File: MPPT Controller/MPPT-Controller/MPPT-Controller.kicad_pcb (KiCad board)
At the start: 4 copper layers, 89 parts, among them J1 Conn_01x02_Pin, J2 Conn_01x02_Pin, J3 Conn_01x02_Pin, J4 Conn_01x02_Pin, J5 USB_C_Receptacle_USB2.0_16P, J6 Conn_01x02_Pin, J7 Conn_01x02_Pin, J8 Conn_01x02_Pin, M1 Fan_4pin, Q1 IRL540N, SW1 SW_SPDT, U1 ADS1115IDGS, U2 ESP32-WROOM-32D, U3 CH340C, U4 LM1117DT-3.3, U5 LM2596S-ADJ, U6 TC4422, U7 ADS1115IDGS

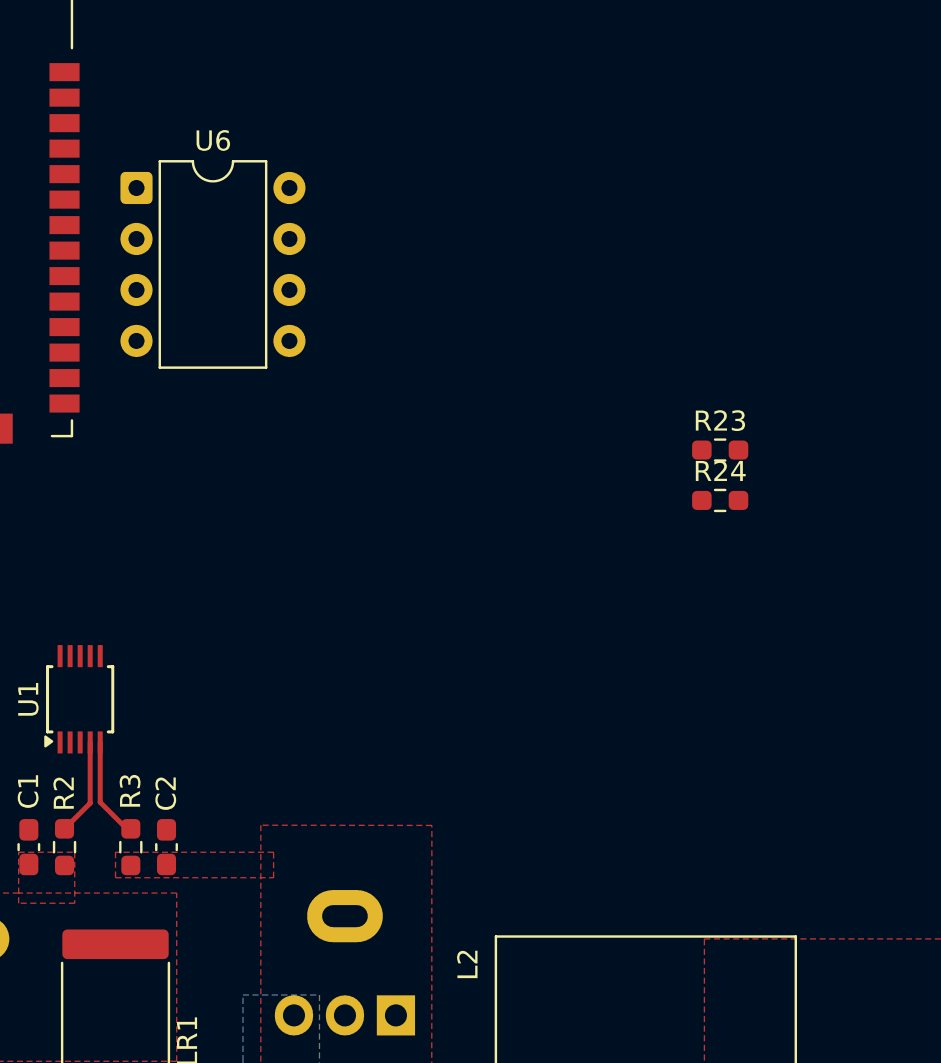
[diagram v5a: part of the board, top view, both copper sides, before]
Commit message: Change Heatsink to 18mm pitch
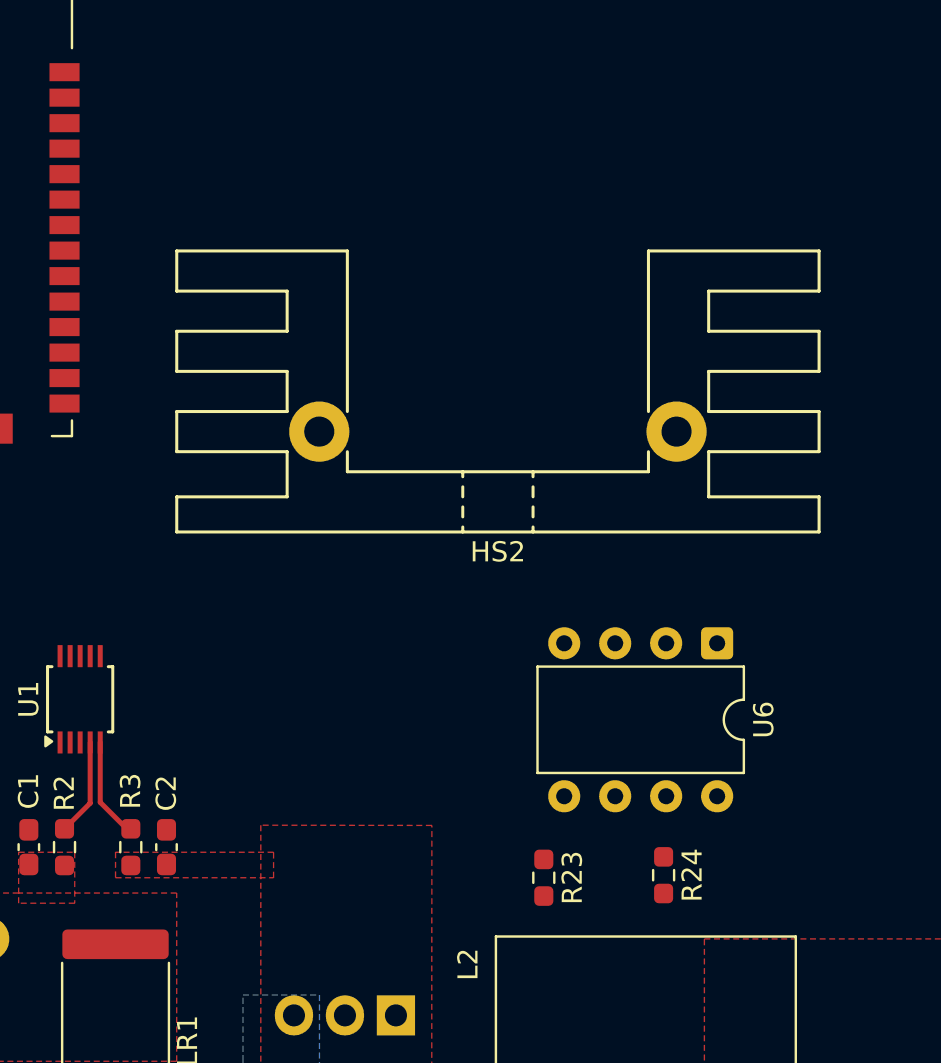
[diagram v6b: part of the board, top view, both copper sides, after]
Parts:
- removed HS1: Heatsink_Pad, Heatsink:Heatsink_AAVID_576802B03900G
- added HS2: Heatsink_Pad_2Pin, Heatsink:Heatsink_Stonecold_HS-132_32x14mm_2xFixation1.5mm, F.Cu at (76.2, 76.3)
- moved U6 36.8 mm to (87.1, 86.9), turned to -90 degrees
- moved R23 23.0 mm to (78.5, 98.6), turned to -90 degrees
- moved R24 18.9 mm to (84.5, 98.4), turned to -90 degrees
